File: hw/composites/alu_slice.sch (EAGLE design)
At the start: 9 parts, among them CON2 GENERIC-2X10

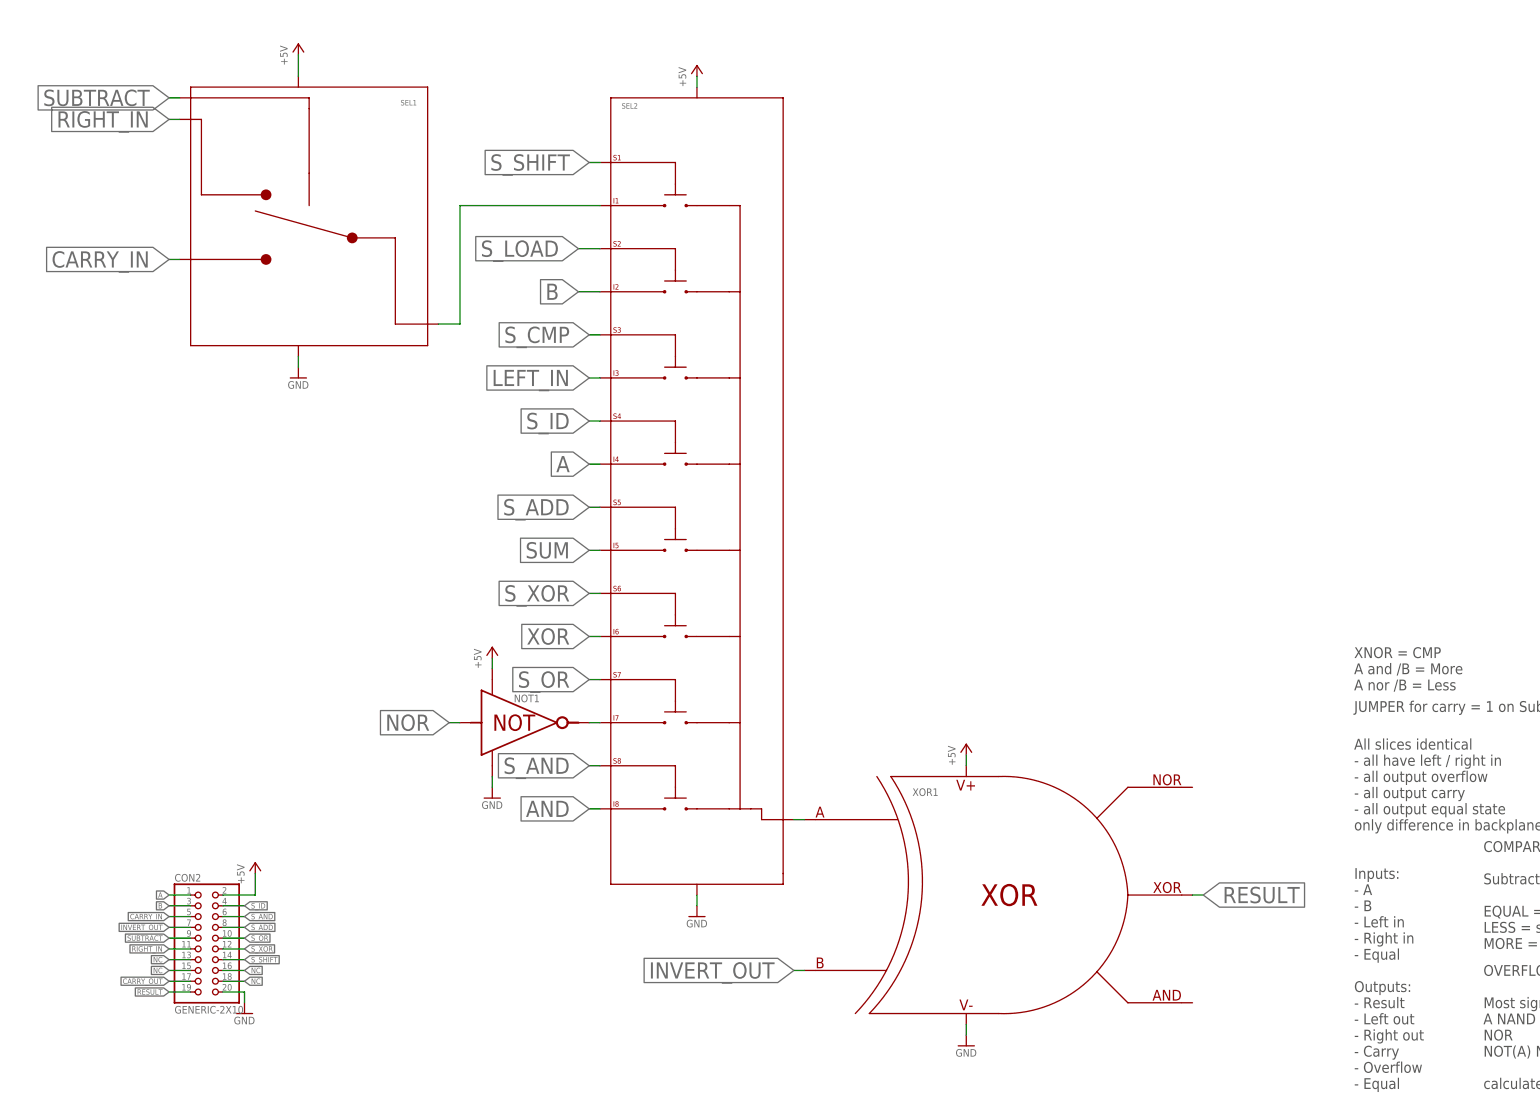
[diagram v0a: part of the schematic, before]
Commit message: Separated input for shift from inputs for addition
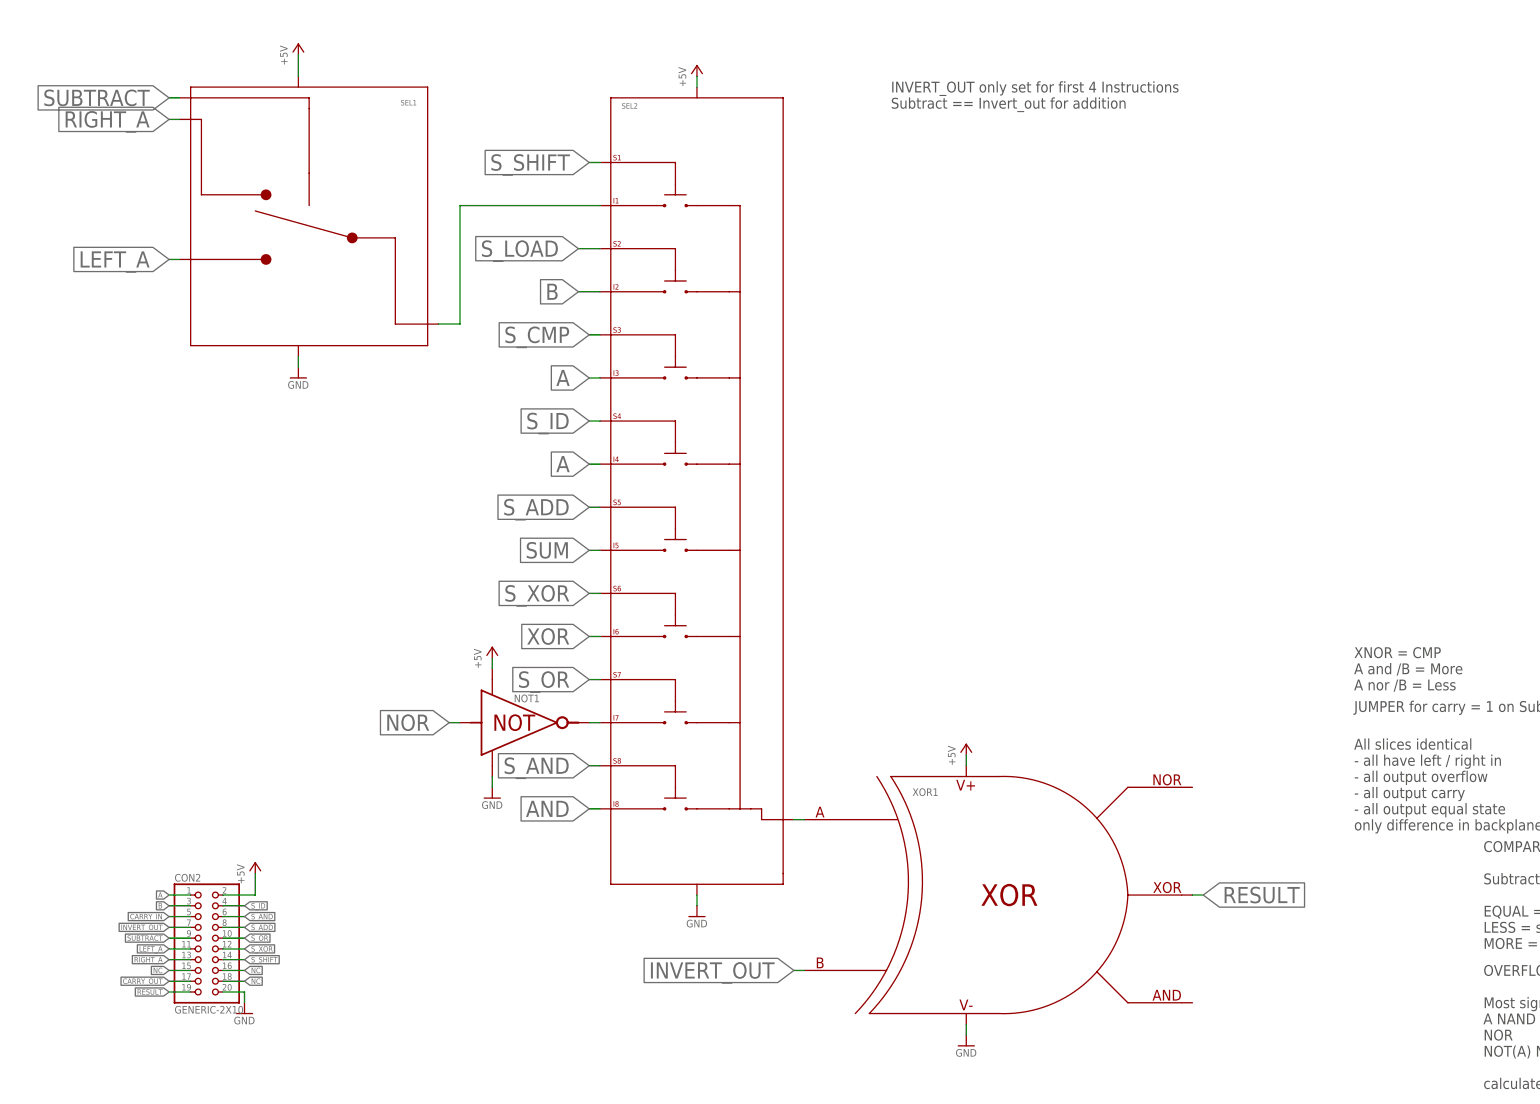
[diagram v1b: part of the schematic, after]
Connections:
- removed net LEFT_IN: SEL2.I3
- removed net RIGHT_IN: CON2.11, SEL1.A
- new net LEFT_A: CON2.11, SEL1.B
- new net RIGHT_A: CON2.13, SEL1.A
- net A: now also SEL2.I3
- net CARRY_IN: no longer SEL1.B
- net NC: no longer CON2.13
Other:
- note added: "INVERT_OUT only set for first 4 Instructions Subtract == Invert_out for addition"
- note removed: "Inputs: - A - B - Left in - Right in - Equal Outputs: - Result - Left out - Right out - Carry - Overflow - Equal"
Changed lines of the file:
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@@
 - all output equal state
 only difference in backplane</text>
-<text x="220.98" y="-91.44" size="2.54" layer="97" ratio="12">Inputs:
-- A
-- B
-- Left in
-- Right in
-- Equal
-Outputs:
-- Result
-- Left out
-- Right out
-- Carry
-- Overflow
-- Equal
-</text>
 <text x="251.46" y="-58.42" size="2.54" layer="97" ratio="12">COMPARE:
 Subtract A - B
@@
 NOT(A) NAND NOT(B) NAND sum
 calculated offsite</text>
+<text x="111.76" y="139.7" size="2.54" layer="97" ratio="12">INVERT_OUT only set for first 4 Instructions
+Subtract == Invert_out for addition
+</text>
 </plain>
 <instances>
@@
 <label x="-58.42" y="-45.72" size="1.27" layer="95" ratio="9" rot="R180" xref="yes"/>
 </segment>
+<segment>
+<pinref part="SEL2" gate="G$1" pin="I3"/>
+<wire x1="43.18" y1="76.2" x2="40.64" y2="76.2" width="0.1524" layer="91"/>
+<label x="40.64" y="76.2" size="3.81" layer="95" ratio="11" rot="R180" xref="yes"/>
+</segment>
 </net>
 <net name="XOR" class="0">
@@
 <label x="-58.42" y="-50.8" size="1.27" layer="95" ratio="9" rot="R180" xref="yes"/>
 </segment>
-<segment>
-<pinref part="SEL1" gate="G$1" pin="B"/>
-<wire x1="-55.88" y1="104.14" x2="-58.42" y2="104.14" width="0.1524" layer="91"/>
-<label x="-58.42" y="104.14" size="3.81" layer="95" ratio="12" rot="R180" xref="yes"/>
-</segment>
 </net>
 <net name="SUM" class="0">
@@
 <wire x1="-53.34" y1="-48.26" x2="-58.42" y2="-48.26" width="0.1524" layer="91"/>
 <label x="-58.42" y="-48.26" size="1.27" layer="95" ratio="9" rot="R180" xref="yes"/>
-</segment>
-</net>
-<net name="LEFT_IN" class="0">
-<segment>
-<pinref part="SEL2" gate="G$1" pin="I3"/>
-<wire x1="43.18" y1="76.2" x2="40.64" y2="76.2" width="0.1524" layer="91"/>
-<label x="40.64" y="76.2" size="3.81" layer="95" ratio="11" rot="R180" xref="yes"/>
 </segment>
 </net>
@@
 <net name="NC" class="0">
 <segment>
-<pinref part="CON2" gate="G$1" pin="13"/>
-<wire x1="-53.34" y1="-60.96" x2="-58.42" y2="-60.96" width="0.1524" layer="91"/>
-<label x="-58.42" y="-60.96" size="1.27" layer="95" ratio="9" rot="R180" xref="yes"/>
-</segment>
-<segment>
 <pinref part="CON2" gate="G$1" pin="15"/>
 <wire x1="-53.34" y1="-63.5" x2="-58.42" y2="-63.5" width="0.1524" layer="91"/>
@@
 <pinref part="NOT1" gate="G$1" pin="NOT"/>
 <wire x1="40.64" y1="-5.08" x2="43.18" y2="-5.08" width="0.1524" layer="91"/>
-</segment>
-</net>
-<net name="RIGHT_IN" class="0">
-<segment>
-<pinref part="CON2" gate="G$1" pin="11"/>
-<wire x1="-53.34" y1="-58.42" x2="-58.42" y2="-58.42" width="0.1524" layer="91"/>
-<label x="-58.42" y="-58.42" size="1.27" layer="95" ratio="9" rot="R180" xref="yes"/>
-</segment>
-<segment>
-<pinref part="SEL1" gate="G$1" pin="A"/>
-<wire x1="-55.88" y1="137.16" x2="-58.42" y2="137.16" width="0.1524" layer="91"/>
-<label x="-58.42" y="137.16" size="3.81" layer="95" ratio="12" rot="R180" xref="yes"/>
 </segment>
 </net>
@@
 </segment>
 </net>
+<net name="RIGHT_A" class="0">
+<segment>
+<pinref part="SEL1" gate="G$1" pin="A"/>
+<wire x1="-55.88" y1="137.16" x2="-58.42" y2="137.16" width="0.1524" layer="91"/>
+<label x="-58.42" y="137.16" size="3.81" layer="95" ratio="12" rot="R180" xref="yes"/>
+</segment>
+<segment>
+<pinref part="CON2" gate="G$1" pin="13"/>
+<wire x1="-53.34" y1="-60.96" x2="-58.42" y2="-60.96" width="0.1524" layer="91"/>
+<label x="-58.42" y="-60.96" size="1.27" layer="95" ratio="9" rot="R180" xref="yes"/>
+</segment>
+</net>
+<net name="LEFT_A" class="0">
+<segment>
+<pinref part="SEL1" gate="G$1" pin="B"/>
+<wire x1="-55.88" y1="104.14" x2="-58.42" y2="104.14" width="0.1524" layer="91"/>
+<label x="-58.42" y="104.14" size="3.81" layer="95" ratio="12" rot="R180" xref="yes"/>
+</segment>
+<segment>
+<pinref part="CON2" gate="G$1" pin="11"/>
+<wire x1="-53.34" y1="-58.42" x2="-58.42" y2="-58.42" width="0.1524" layer="91"/>
+<label x="-58.42" y="-58.42" size="1.27" layer="95" ratio="9" rot="R180" xref="yes"/>
+</segment>
+</net>

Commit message: adds additional tests for offloading of CMP on slice
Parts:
- added OR2: OR, p.peter-gator:OR
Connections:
- new net _EQUAL_IN: CON2.15, OR2.A
- new net _EQUAL_OUT: CON2.19, OR2.OR
- net +5V: now also OR2._VP
- net GND: now also OR2._VN
- net NC: no longer CON2.15, CON2.18
- net RESULT: now also CON2.18; no longer CON2.19
- net SUM: now also OR2.B
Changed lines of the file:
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@@
 <part name="GND5" library="supply1" deviceset="GND" device=""/>
 <part name="P+5" library="supply1" deviceset="+5V" device=""/>
+<part name="OR2" library="p.peter-gator" deviceset="OR" device=""/>
+<part name="P+6" library="supply1" deviceset="+5V" device=""/>
+<part name="GND6" library="supply1" deviceset="GND" device=""/>
 </parts>
 <sheets>
@@
 <instance part="GND5" gate="1" x="-27.94" y="76.2"/>
 <instance part="P+5" gate="1" x="-27.94" y="154.94"/>
+<instance part="OR2" gate="G$1" x="312.42" y="259.08"/>
+<instance part="P+6" gate="1" x="299.72" y="292.1"/>
+<instance part="GND6" gate="1" x="299.72" y="226.06"/>
 </instances>
 <busses>
@@
 <segment>
 <pinref part="XOR3" gate="G$1" pin="XOR"/>
-<wire x1="241.3" y1="246.38" x2="294.64" y2="246.38" width="0.1524" layer="91"/>
-<label x="294.64" y="246.38" size="3.81" layer="95" ratio="12" xref="yes"/>
+<wire x1="241.3" y1="246.38" x2="243.84" y2="246.38" width="0.1524" layer="91"/>
+<wire x1="243.84" y1="246.38" x2="243.84" y2="251.46" width="0.1524" layer="91"/>
+<wire x1="243.84" y1="251.46" x2="246.38" y2="251.46" width="0.1524" layer="91"/>
+<label x="246.38" y="251.46" size="3.81" layer="95" ratio="12" xref="yes"/>
+<pinref part="OR2" gate="G$1" pin="B"/>
+<wire x1="243.84" y1="246.38" x2="284.48" y2="246.38" width="0.1524" layer="91"/>
+<junction x="243.84" y="246.38"/>
 </segment>
 </net>
@@
 <wire x1="-27.94" y1="152.4" x2="-27.94" y2="147.32" width="0.1524" layer="91"/>
 </segment>
+<segment>
+<pinref part="OR2" gate="G$1" pin="_VP"/>
+<pinref part="P+6" gate="1" pin="+5V"/>
+<wire x1="299.72" y1="289.56" x2="299.72" y2="287.02" width="0.1524" layer="91"/>
+</segment>
 </net>
 <net name="GND" class="0">
@@
 <pinref part="GND5" gate="1" pin="GND"/>
 <wire x1="-27.94" y1="81.28" x2="-27.94" y2="78.74" width="0.1524" layer="91"/>
+</segment>
+<segment>
+<pinref part="OR2" gate="G$1" pin="_VN"/>
+<pinref part="GND6" gate="1" pin="GND"/>
+<wire x1="299.72" y1="228.6" x2="299.72" y2="231.14" width="0.1524" layer="91"/>
 </segment>
 </net>
@@
 <net name="RESULT" class="0">
 <segment>
-<pinref part="CON2" gate="G$1" pin="19"/>
-<wire x1="-53.34" y1="-68.58" x2="-58.42" y2="-68.58" width="0.1524" layer="91"/>
-<label x="-58.42" y="-68.58" size="1.27" layer="95" ratio="9" rot="R180" xref="yes"/>
+<pinref part="CON2" gate="G$1" pin="18"/>
+<wire x1="-45.72" y1="-66.04" x2="-40.64" y2="-66.04" width="0.1524" layer="91"/>
+<label x="-40.64" y="-66.04" size="1.27" layer="95" ratio="9" xref="yes"/>
 </segment>
 <segment>
@@
 <net name="NC" class="0">
 <segment>
-<pinref part="CON2" gate="G$1" pin="15"/>
-<wire x1="-53.34" y1="-63.5" x2="-58.42" y2="-63.5" width="0.1524" layer="91"/>
-<label x="-58.42" y="-63.5" size="1.27" layer="95" ratio="9" rot="R180" xref="yes"/>
-</segment>
-<segment>
 <pinref part="CON2" gate="G$1" pin="16"/>
 <wire x1="-45.72" y1="-63.5" x2="-40.64" y2="-63.5" width="0.1524" layer="91"/>
 <label x="-40.64" y="-63.5" size="1.27" layer="95" ratio="9" xref="yes"/>
-</segment>
-<segment>
-<pinref part="CON2" gate="G$1" pin="18"/>
-<wire x1="-45.72" y1="-66.04" x2="-40.64" y2="-66.04" width="0.1524" layer="91"/>
-<label x="-40.64" y="-66.04" size="1.27" layer="95" ratio="9" xref="yes"/>
 </segment>
 </net>
@@
 </segment>
 </net>
+<net name="_EQUAL_IN" class="0">
+<segment>
+<pinref part="OR2" gate="G$1" pin="A"/>
+<wire x1="284.48" y1="271.78" x2="281.94" y2="271.78" width="0.1524" layer="91"/>
+<label x="281.94" y="271.78" size="3.81" layer="95" ratio="12" rot="R180" xref="yes"/>
+</segment>
+<segment>
+<pinref part="CON2" gate="G$1" pin="15"/>
+<wire x1="-53.34" y1="-63.5" x2="-58.42" y2="-63.5" width="0.1524" layer="91"/>
+<label x="-58.42" y="-63.5" size="1.27" layer="95" ratio="9" rot="R180" xref="yes"/>
+</segment>
+</net>
+<net name="_EQUAL_OUT" class="0">
+<segment>
+<pinref part="OR2" gate="G$1" pin="OR"/>
+<wire x1="335.28" y1="259.08" x2="332.74" y2="259.08" width="0.1524" layer="91"/>
+<label x="335.28" y="259.08" size="3.81" layer="95" ratio="12" xref="yes"/>
+</segment>
+<segment>
+<pinref part="CON2" gate="G$1" pin="19"/>
+<wire x1="-53.34" y1="-68.58" x2="-58.42" y2="-68.58" width="0.1524" layer="91"/>
+<label x="-58.42" y="-68.58" size="1.27" layer="95" ratio="9" rot="R180" xref="yes"/>
+</segment>
+</net>

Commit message: cleans up board layout
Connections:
- removed net NC: CON2.16
- net S_LOAD: now also CON2.16
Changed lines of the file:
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@@
 <label x="38.1" y="106.68" size="3.81" layer="95" ratio="11" rot="R180" xref="yes"/>
+</segment>
+<segment>
+<pinref part="CON2" gate="G$1" pin="16"/>
+<wire x1="-45.72" y1="-63.5" x2="-40.64" y2="-63.5" width="0.1524" layer="91"/>
+<label x="-40.64" y="-63.5" size="1.27" layer="95" ratio="9" xref="yes"/>
 </segment>
 </net>
@@
 </segment>
 </net>
-<net name="NC" class="0">
-<segment>
-<pinref part="CON2" gate="G$1" pin="16"/>
-<wire x1="-45.72" y1="-63.5" x2="-40.64" y2="-63.5" width="0.1524" layer="91"/>
-<label x="-40.64" y="-63.5" size="1.27" layer="95" ratio="9" xref="yes"/>
-</segment>
-</net>
